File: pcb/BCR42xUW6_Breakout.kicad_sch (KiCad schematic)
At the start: 4 parts, among them J1 Conn_01x03_Male, J2 Conn_01x03_Male, U1 BCR42XUW6

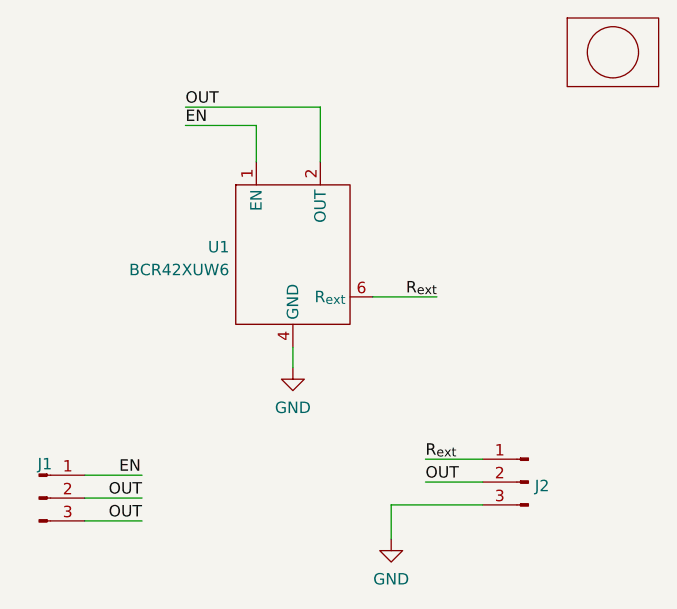
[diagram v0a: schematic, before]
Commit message: Fixes the dimensions of the symbol
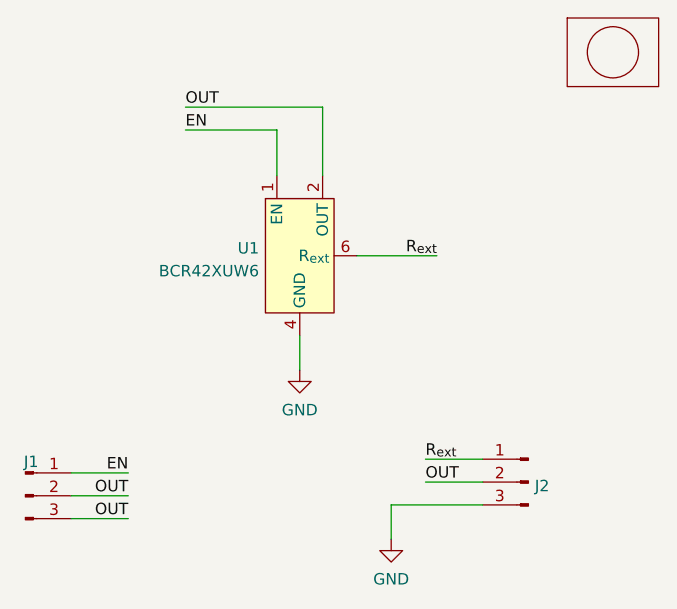
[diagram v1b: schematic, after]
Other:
- moved on the sheet: J1
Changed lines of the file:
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@@
 (kicad_sch (version 20211123) (generator eeschema)
   (paper "A4")
-  (wire (pts (xy 137.668 71.882) (xy 144.78 71.882))
+  (wire (pts (xy 104.14 93.98) (xy 110.49 93.98))
     (stroke (width 0) (type default) (color 0 0 0 0))
   )
-  (wire (pts (xy 105.664 94.234) (xy 112.014 94.234))
-    (stroke (width 0) (type default) (color 0 0 0 0))
-  )
-  (wire (pts (xy 105.664 91.694) (xy 112.014 91.694))
-    (stroke (width 0) (type default) (color 0 0 0 0))
-  )
-  (wire (pts (xy 128.778 77.47) (xy 128.778 79.756))
+  (wire (pts (xy 132.08 50.8) (xy 116.84 50.8))
     (stroke (width 0) (type default) (color 0 0 0 0))
   )
@@
     (stroke (width 0) (type default) (color 0 0 0 0))
   )
-  (wire (pts (xy 105.664 96.774) (xy 112.014 96.774))
+  (wire (pts (xy 127 58.42) (xy 127 53.34))
+    (stroke (width 0) (type default) (color 0 0 0 0))
+  )
+  (wire (pts (xy 104.14 96.52) (xy 110.49 96.52))
+    (stroke (width 0) (type default) (color 0 0 0 0))
+  )
+  (wire (pts (xy 129.54 76.2) (xy 129.54 80.01))
+    (stroke (width 0) (type default) (color 0 0 0 0))
+  )
+  (wire (pts (xy 116.84 53.34) (xy 127 53.34))
+    (stroke (width 0) (type default) (color 0 0 0 0))
+  )
+  (wire (pts (xy 104.14 91.44) (xy 110.49 91.44))
     (stroke (width 0) (type default) (color 0 0 0 0))
   )
@@
     (stroke (width 0) (type default) (color 0 0 0 0))
   )
-  (wire (pts (xy 139.7 94.996) (xy 149.86 94.996))
+  (wire (pts (xy 132.08 58.42) (xy 132.08 50.8))
     (stroke (width 0) (type default) (color 0 0 0 0))
   )
-  (wire (pts (xy 124.714 56.896) (xy 124.714 52.832))
-    (stroke (width 0) (type default) (color 0 0 0 0))
-  )
-  (wire (pts (xy 116.84 50.8) (xy 131.826 50.8))
-    (stroke (width 0) (type default) (color 0 0 0 0))
-  )
-  (wire (pts (xy 116.84 52.832) (xy 124.714 52.832))
+  (wire (pts (xy 139.7 94.996) (xy 149.86 94.996))
     (stroke (width 0) (type default) (color 0 0 0 0))
   )
@@
     (stroke (width 0) (type default) (color 0 0 0 0))
   )
-  (wire (pts (xy 131.826 56.896) (xy 131.826 50.8))
+  (wire (pts (xy 135.89 67.31) (xy 144.78 67.31))
     (stroke (width 0) (type default) (color 0 0 0 0))
   )
-  (label "R_{ext}" (at 144.78 71.882 180)
+  (label "R_{ext}" (at 144.78 67.31 180)
     (effects (font (size 1.27 1.27)) (justify right bottom))
   )
@@
     (effects (font (size 1.27 1.27)) (justify left bottom))
   )
-  (label "OUT" (at 112.014 94.234 180)
+  (label "OUT" (at 110.49 93.98 180)
     (effects (font (size 1.27 1.27)) (justify right bottom))
   )
-  (label "OUT" (at 112.014 96.774 180)
+  (label "OUT" (at 110.49 96.52 180)
     (effects (font (size 1.27 1.27)) (justify right bottom))
   )
-  (label "EN" (at 116.84 52.832 0)
+  (label "EN" (at 116.84 53.34 0)
     (effects (font (size 1.27 1.27)) (justify left bottom))
   )
@@
     (effects (font (size 1.27 1.27)) (justify left bottom))
   )
-  (label "EN" (at 109.474 91.694 0)
-    (effects (font (size 1.27 1.27)) (justify left bottom))
+  (label "EN" (at 110.49 91.44 180)
+    (effects (font (size 1.27 1.27)) (justify right bottom))
+  )
+  (symbol (lib_id "BCR42xUW6:BCR42XUW6") (at 129.54 67.31 0) (unit 1)
+    (in_bom yes) (on_board yes) (fields_autoplaced)
+    (property "Reference" "U1" (id 0) (at 125.0188 66.4753 0)
+      (effects (font (size 1.27 1.27)) (justify right))
+    )
+    (property "Value" "BCR42XUW6" (id 1) (at 125.0188 69.0122 0)
+      (effects (font (size 1.27 1.27)) (justify right))
+    )
+    (property "Footprint" "Package_TO_SOT_SMD:SOT-23-6" (id 2) (at 130.81 78.74 0)
+      (effects (font (size 1.27 1.27)) hide)
+    )
+    (property "Datasheet" "" (id 3) (at 129.54 67.31 0)
+      (effects (font (size 1.27 1.27)) hide)
+    )
+    (pin "1")
+    (pin "2")
+    (pin "3")
+    (pin "4")
+    (pin "5")
+    (pin "6")
   )
   (symbol (lib_id "power:GND") (at 139.7 98.806 0) (unit 1)
@@
     (pin "1")
   )
-  (symbol (lib_id "Connector:Conn_01x03_Male") (at 100.584 94.234 0) (unit 1)
-    (in_bom yes) (on_board yes) (fields_autoplaced)
-    (property "Reference" "J1" (id 0) (at 101.219 90.455 0))
-    (property "Value" "Conn_01x03_Male" (id 1) (at 101.219 90.4549 0)
+  (symbol (lib_id "Connector:Conn_01x03_Male") (at 99.06 93.98 0) (unit 1)
+    (in_bom yes) (on_board yes)
+    (property "Reference" "J1" (id 0) (at 99.695 90.201 0))
+    (property "Value" "Conn_01x03_Male" (id 1) (at 99.695 90.2009 0)
       (effects (font (size 1.27 1.27)) hide)
     )
-    (property "Footprint" "Connector_PinHeader_2.54mm:PinHeader_1x03_P2.54mm_Vertical" (id 2) (at 100.584 94.234 0)
+    (property "Footprint" "Connector_PinHeader_2.54mm:PinHeader_1x03_P2.54mm_Vertical" (id 2) (at 99.06 93.98 0)
       (effects (font (size 1.27 1.27)) hide)
     )
-    (property "Datasheet" "~" (id 3) (at 100.584 94.234 0)
+    (property "Datasheet" "~" (id 3) (at 99.06 93.98 0)
       (effects (font (size 1.27 1.27)) hide)
     )
@@
     )
   )
-  (symbol (lib_id "power:GND") (at 128.778 79.756 0) (unit 1)
+  (symbol (lib_id "power:GND") (at 129.54 80.01 0) (unit 1)
     (in_bom yes) (on_board yes) (fields_autoplaced)
-    (property "Reference" "#PWR01" (id 0) (at 128.778 86.106 0)
+    (property "Reference" "#PWR01" (id 0) (at 129.54 86.36 0)
       (effects (font (size 1.27 1.27)) hide)
     )
-    (property "Value" "GND" (id 1) (at 128.778 84.1994 0))
-    (property "Footprint" "" (id 2) (at 128.778 79.756 0)
+    (property "Value" "GND" (id 1) (at 129.54 84.4534 0))
+    (property "Footprint" "" (id 2) (at 129.54 80.01 0)
       (effects (font (size 1.27 1.27)) hide)
     )
-    (property "Datasheet" "" (id 3) (at 128.778 79.756 0)
+    (property "Datasheet" "" (id 3) (at 129.54 80.01 0)
       (effects (font (size 1.27 1.27)) hide)
     )
     (pin "1")
-  )
-  (symbol (lib_id "BCR42xUW6:BCR42XUW6") (at 128.778 67.818 0) (unit 1)
-    (in_bom yes) (on_board yes) (fields_autoplaced)
-    (property "Reference" "U1" (id 0) (at 121.7168 66.3483 0)
-      (effects (font (size 1.27 1.27)) (justify right))
-    )
-    (property "Value" "BCR42XUW6" (id 1) (at 121.7168 68.8852 0)
-      (effects (font (size 1.27 1.27)) (justify right))
-    )
-    (property "Footprint" "Package_TO_SOT_SMD:SOT-23-6" (id 2) (at 128.778 67.818 0)
-      (effects (font (size 1.27 1.27)) hide)
-    )
-    (property "Datasheet" "" (id 3) (at 128.778 67.818 0)
-      (effects (font (size 1.27 1.27)) hide)
-    )
-    (property "Reference" "U1" (id 4) (at 128.778 67.818 0)
-      (effects (font (size 1.27 1.27)) hide)
-    )
-    (property "Value" "BCR42XUW6" (id 5) (at 128.778 67.818 0)
-      (effects (font (size 1.27 1.27)) hide)
-    )
-    (pin "1")
-    (pin "2")
-    (pin "3")
-    (pin "4")
-    (pin "5")
-    (pin "6")
   )
   (symbol (lib_id "Connector:Conn_01x03_Male") (at 154.94 92.456 0) (mirror y) (unit 1)
@@
       (reference "Lg1") (unit 1) (value "logo") (footprint "mech:MyBasic_rounded_50_1")
     )
-    (path "/ed3c769f-c5e4-4fda-a79e-255a4e2e889c"
+    (path "/00ecc8fc-87dd-48dc-9ce7-c0d851e83f46"
       (reference "U1") (unit 1) (value "BCR42XUW6") (footprint "Package_TO_SOT_SMD:SOT-23-6")
     )
